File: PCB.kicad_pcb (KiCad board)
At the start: 2 copper layers, 86 x 156.5 mm, 30 parts, among them J1 Conn_01x04, J2 Screw_Terminal_01x02, J3 Screw_Terminal_01x05, J4 Screw_Terminal_01x05, K1 G5LE-1A_DC3, K2 G5LE-1A_DC3, K3 G5LE-1, K4 G5LE-1, K6 G5LE-1, K7 G5LE-1A_DC3, Q1 DMN65D8L-7, Q2 DMN65D8L-7, Q3 DMN65D8L-7, SW1 Local DI0 (onoff), SW3 Local DI2 (decspeed), SW4 local/remote switch, SW5 Local DI1 (incspeed), U1 WeMos_D1_mini

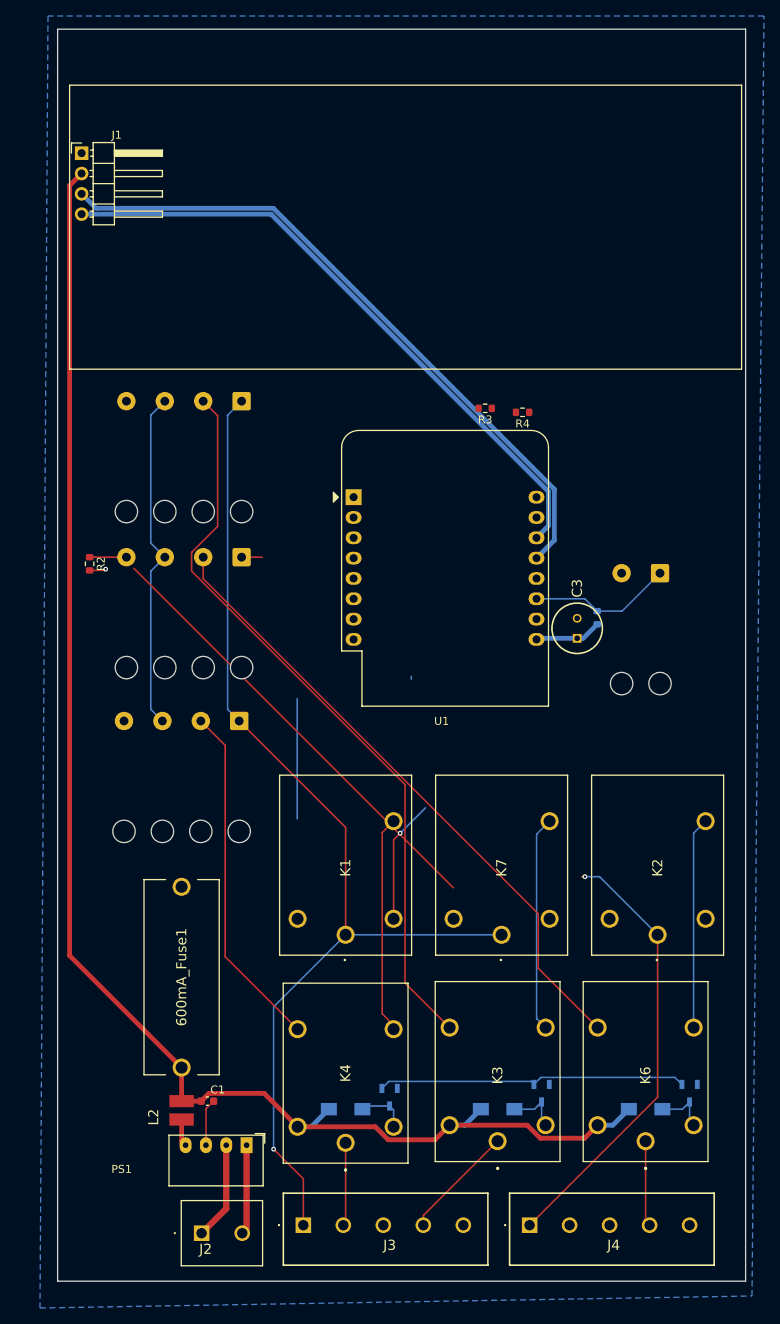
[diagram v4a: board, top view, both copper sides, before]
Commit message: aktualizace pcb na zaklade predeslych oprav
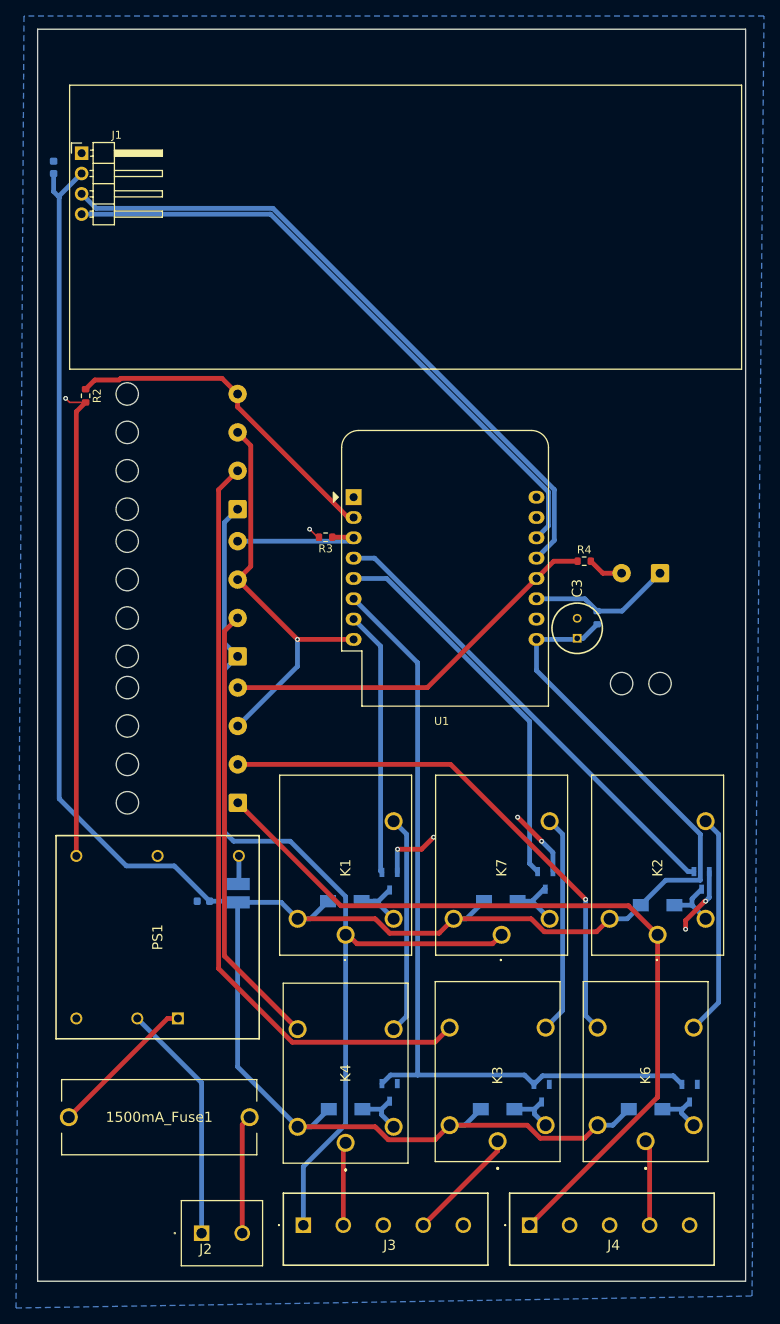
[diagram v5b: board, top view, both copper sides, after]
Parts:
- removed 600mA_Fuse1: 0PTF0078P, 600 mA fuse:0PTF0078P
- added 1500mA_Fuse1: 0PTF0078P, 600 mA fuse:0PTF0078P, F.Cu at (75.2, 201.0)
- added C2: 10uF, Capacitor_SMD:C_0603_1608Metric, B.Cu at (62.0, 82.3)
- added D4: SK16, schottky:DIOM5027X250N, B.Cu at (117.9, 174.0)
- added D5: SK16, schottky:DIOM5027X250N, B.Cu at (98.4, 174.0)
- added D6: SK16, schottky:DIOM5027X250N, B.Cu at (137.5, 174.5)
- added Q4: DMN65D8L-7, mosfet:SOT96P240X115-3N, B.Cu at (123.5, 171.4)
- added Q5: DMN65D8L-7, mosfet:SOT96P240X115-3N, B.Cu at (104.0, 171.5)
- added Q6: DMN65D8L-7, mosfet:SOT96P240X115-3N, B.Cu at (143.0, 171.4)
- C1, L2: moved to B.Cu
- PS1: value CRE1S2405SC -> REC10K-2405SAW_H2; footprint Converter_DCDC:Converter_DCDC_Murata_CRE1xxxxxxSC_THT -> dcdc converter:REC10K-AW
- moved SW3 30.7 mm to (85.0, 161.7), turned to 90 degrees
- moved PS1 28.3 mm to (75.0, 178.5), turned to 90 degrees
- moved L2 28.0 mm to (85.0, 173.0), turned to -90 degrees
- moved R3 25.6 mm to (96.0, 128.5)
- moved C1 25.0 mm to (80.7, 174.0), turned to 180 degrees
- moved R2 21.0 mm to (66.0, 110.8)
- moved R4 20.1 mm to (128.3, 131.5), turned to 0 degrees
- moved SW1 13.5 mm to (85.0, 125.0), turned to 90 degrees
- moved SW5 8.08 mm to (85.0, 143.4), turned to 90 degrees
- moved Q2 0.60 mm to (104.0, 197.9)
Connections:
- C3 pad 1: Net-(C3-+) -> VCC
- K1 pad 2: DO6 -> Net-(D5-A)
- K1 pad 5: GND -> VCC
- K2 pad 2: DO7 -> Net-(D6-A)
- K2 pad 5: GND -> VCC
- K7 pad 2: DO5 -> Net-(D4-A)
- K7 pad 5: GND -> VCC
- PS1 pad 1: Net-(J2-Pin_2) -> Net-(PS1-+VIN)
- PS1 pad 3: GND -> unconnected-(PS1-CTRL-Pad3)
- PS1 pad 4: Net-(PS1-+VOUT) -> GND
- R1 pad 1: Net-(C3-+) -> VCC
- R2 pad 1: DO3 -> DOA
- R4 pad 1: DOA -> DO3
- U1 pad 4: DO5 -> DO7
- U1 pad 5: DO6 -> DO5
- U1 pad 6: DO7 -> DO8
- U1 pad 7: DO8 -> DO6
- U1 pad 9: Net-(C3-+) -> VCC
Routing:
- net VCC: track 193.6 -> 315.8 mm
- net GND: track 8.31 -> 91.1 mm, vias 1 -> 8
- net DO8: track 38.7 -> 102.2 mm
- net DO7: track 0.00 -> 58.8 mm
- net DO5: track 0.00 -> 48.6 mm
- net DO3: track 4.60 -> 49.0 mm
- net DOA: track 0.00 -> 42.2 mm
- net Net-(PS1-+VIN): track 0.00 -> 18.8 mm
- net Net-(J2-Pin_1): track 12.3 -> 30.2 mm
- net DO0: track 0.00 -> 17.4 mm
- net local DI1: track 43.5 -> 55.9 mm
- net J4 24V: track 114.5 -> 102.2 mm, vias 1 -> 0
- net local DI2: track 79.2 -> 67.1 mm, vias 0 -> 1
- net J3 24V: track 134.6 -> 124.6 mm, vias 1 -> 0
- net MCU 3V3: track 42.8 -> 51.3 mm, vias 0 -> 1
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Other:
- board size 86 x 156.5 mm -> 88.5 x 156.5 mm

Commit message: aktualizace par jmen ve schematu a prave jdu na updatovani pcb
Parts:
- added H1: MountingHole, MountingHole:MountingHole_5mm, B.Cu at (131.5, 115.5)
- added H10: MountingHole, MountingHole:MountingHole_5mm, B.Cu at (140.5, 73.5)
- added H11: MountingHole, MountingHole:MountingHole_5mm, B.Cu at (82.0, 72.5)
- added H2: MountingHole, MountingHole:MountingHole_5mm, F.Cu at (68.5, 214.0)
- added H3: MountingHole, MountingHole:MountingHole_4mm, B.Cu at (93.0, 152.0)
- added H4: MountingHole, MountingHole:MountingHole_5mm, B.Cu at (142.0, 124.0)
- added H5: MountingHole, MountingHole:MountingHole_4mm, B.Cu at (142.5, 152.0)
- added H6: MountingHole, MountingHole:MountingHole_4mm, B.Cu at (93.0, 113.0)
- added H7: MountingHole, MountingHole:MountingHole_3mm, B.Cu at (109.0, 153.0)
- added H8: MountingHole, MountingHole:MountingHole_4mm, F.Cu at (128.0, 152.5)
- added H9: MountingHole, MountingHole:MountingHole_4mm, B.Cu at (93.0, 134.5)
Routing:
- net GND: track 91.1 -> 75.8 mm, vias 8 -> 7
- net SDA: track 83.9 -> 89.4 mm
- net SCL: track 79.1 -> 84.6 mm
- net local DI2: track 67.1 -> 72.5 mm
- net DO8: track 102.2 -> 107.4 mm
- net MCU 3V3: track 51.3 -> 56.3 mm, vias 1 -> 0
- net DO5: track 48.6 -> 46.2 mm
- net VCC: track 315.8 -> 313.9 mm
- net DO7: track 58.8 -> 59.7 mm

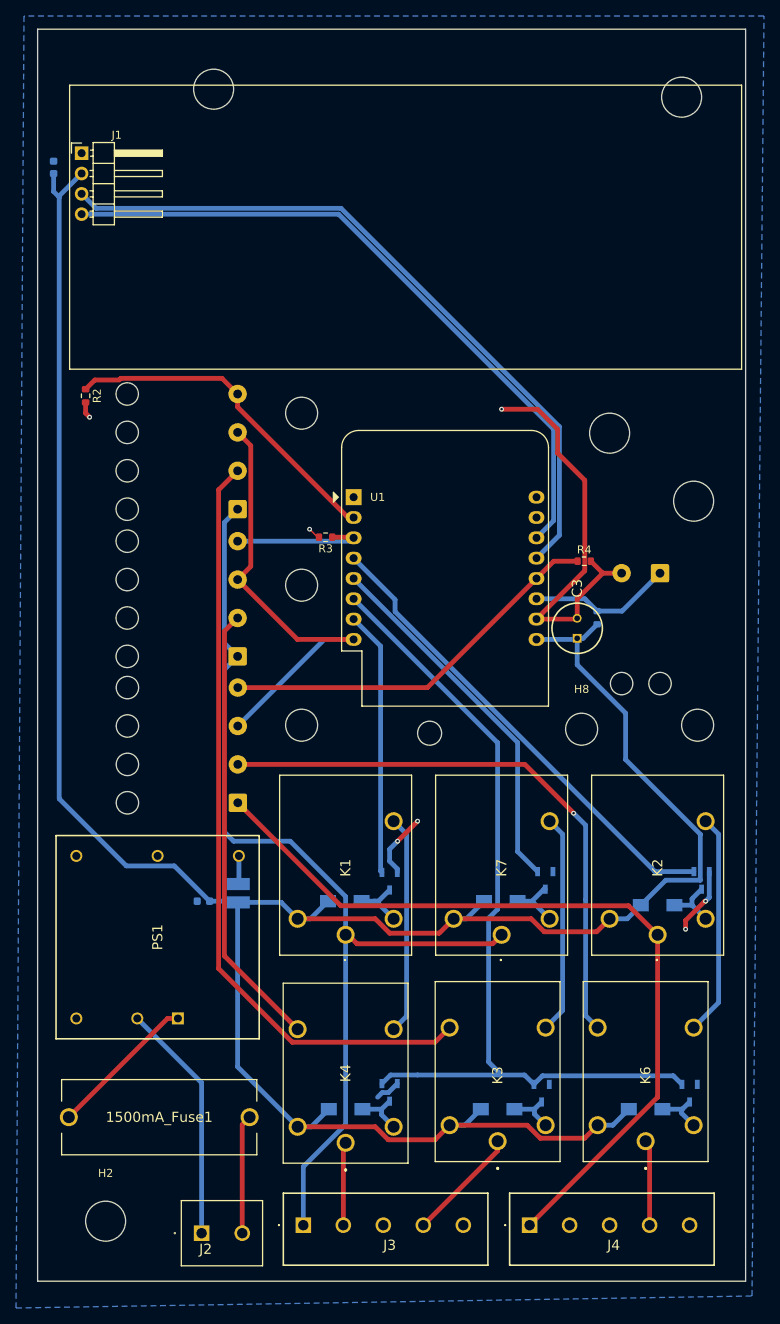
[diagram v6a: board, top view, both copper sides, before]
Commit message: prvni aktualizace jmen done
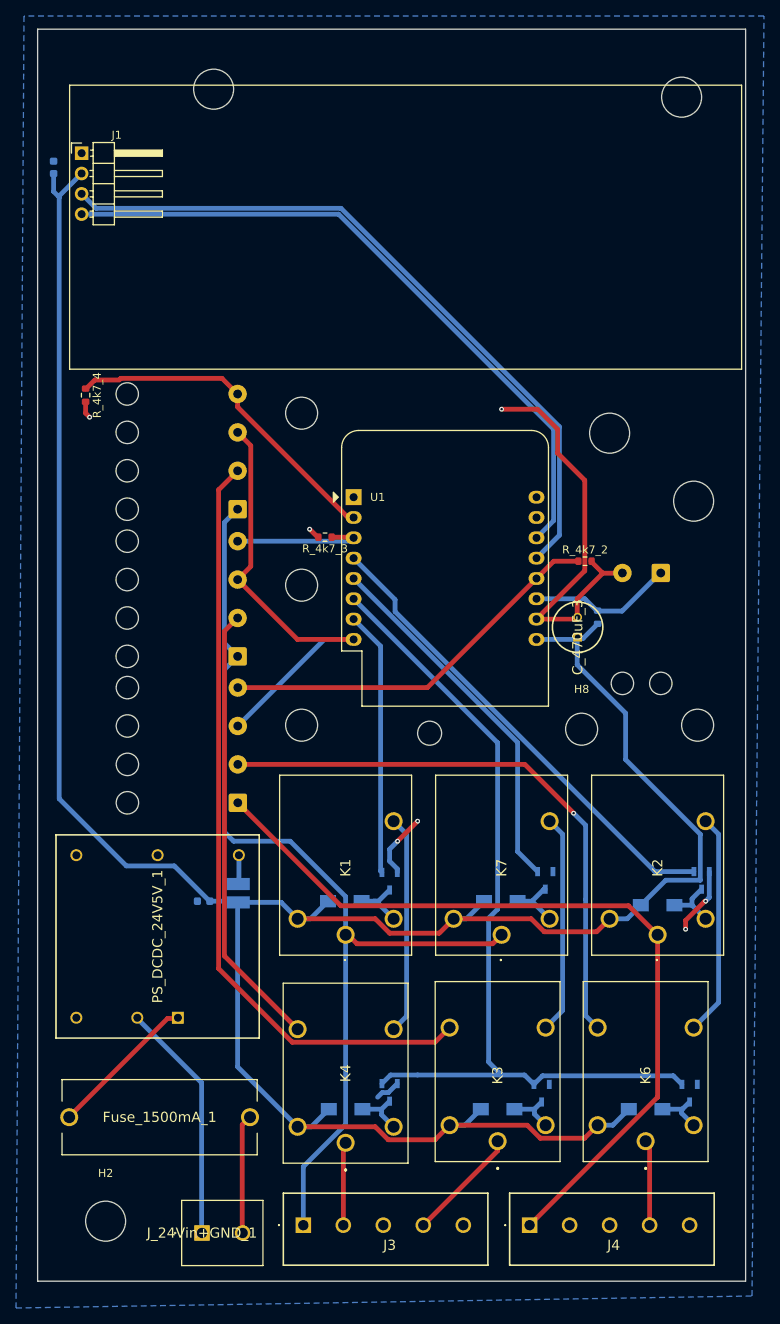
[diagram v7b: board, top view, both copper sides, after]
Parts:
- removed 1500mA_Fuse1: 0PTF0078P, 600 mA fuse:0PTF0078P
- removed C1: 22uF, Capacitor_SMD:C_0603_1608Metric
- removed C3: 470uF, 470uF C:CAPPRD250W52D630H1250
- removed J2: Screw_Terminal_01x02, 1x2 screw conn:1729128
- removed L2: 82103C 10uH, DCDC L:8200
- removed PS1: REC10K-2405SAW_H2, dcdc converter:REC10K-AW
- removed R1, R2, R3, R4: 4k7, Resistor_SMD:R_0603_1608Metric
- removed SW4: local/remote switch, Connector_Wire:SolderWire-0.5sqmm_1x02_P4.8mm_D0.9mm_OD2.3mm_Relief
- added C_22uF_1: 22uF, Capacitor_SMD:C_0603_1608Metric, B.Cu at (80.8, 174.0)
- added C_470uF_3: 470uF, 470uF C:CAPPRD250W52D630H1250, F.Cu at (127.5, 141.0)
- added Fuse_1500mA_1: 0PTF0078P, 600 mA fuse:0PTF0078P, F.Cu at (75.2, 201.0)
- added J_24Vin+GND_1: Screw_Terminal_01x02, 1x2 screw conn:1729128, F.Cu at (80.5, 215.5)
- added L_10uH_1: 82103C 10uH, DCDC L:8200, B.Cu at (85.0, 173.0)
- added PS_DCDC_24V5V_1: REC10K-2405SAW_H2, dcdc converter:REC10K-AW, F.Cu at (75.0, 178.4)
- added R_4k7_1: 4k7, Resistor_SMD:R_0603_1608Metric, B.Cu at (130.0, 138.5)
- added R_4k7_2: 4k7, Resistor_SMD:R_0603_1608Metric, F.Cu at (128.4, 131.5)
- added R_4k7_3: 4k7, Resistor_SMD:R_0603_1608Metric, F.Cu at (95.9, 128.5)
- added R_4k7_4: 4k7, Resistor_SMD:R_0603_1608Metric, F.Cu at (66.0, 110.8)
- added SW_LocRem_1: local/remote switch, Connector_Wire:SolderWire-0.5sqmm_1x02_P4.8mm_D0.9mm_OD2.3mm_Relief, B.Cu at (137.9, 133.0)
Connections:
- Q1 pad 1: DO8 -> DO7
- Q2 pad 1: DO8 -> DO7
- Q3 pad 1: DO8 -> DO7
- Q4 pad 1: DO5 -> DO6
- Q5 pad 1: DO6 -> DO8
- Q6 pad 1: DO7 -> DO5
- U1 pad 4: DO7 -> DO5
- U1 pad 5: DO5 -> DO6
- U1 pad 6: DO8 -> DO7
- U1 pad 7: DO6 -> DO8
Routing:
- net DO8: track 107.4 -> 33.1 mm
- net DO7: track 59.7 -> 107.4 mm
- net Net-(J_24Vin+GND_1-Pin_1): track 0.00 -> 30.2 mm
- net Net-(J2-Pin_1): track 30.2 -> 0.00 mm
- net Net-(PS_DCDC_24V5V_1-+VIN): track 0.00 -> 18.8 mm
- net Net-(PS1-+VIN): track 18.8 -> 0.00 mm
- net Net-(J_24Vin+GND_1-Pin_2): track 0.00 -> 14.9 mm
- net Net-(J2-Pin_2): track 14.9 -> 0.00 mm
- net DO5: track 46.2 -> 59.7 mm
- net DO6: track 33.1 -> 46.2 mm
- net Net-(PS_DCDC_24V5V_1-+VOUT): track 0.00 -> 3.58 mm
- net Net-(PS1-+VOUT): track 3.58 -> 0.00 mm
